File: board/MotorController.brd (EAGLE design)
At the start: 88.9 x 54.6 mm, 41 parts, among them IC1 ATMEGA328P-PU, Q1 IPP80P03P4L-04, Q2 SUP75P03-07-H, T1 BT137-600E, Y1 16Mhz

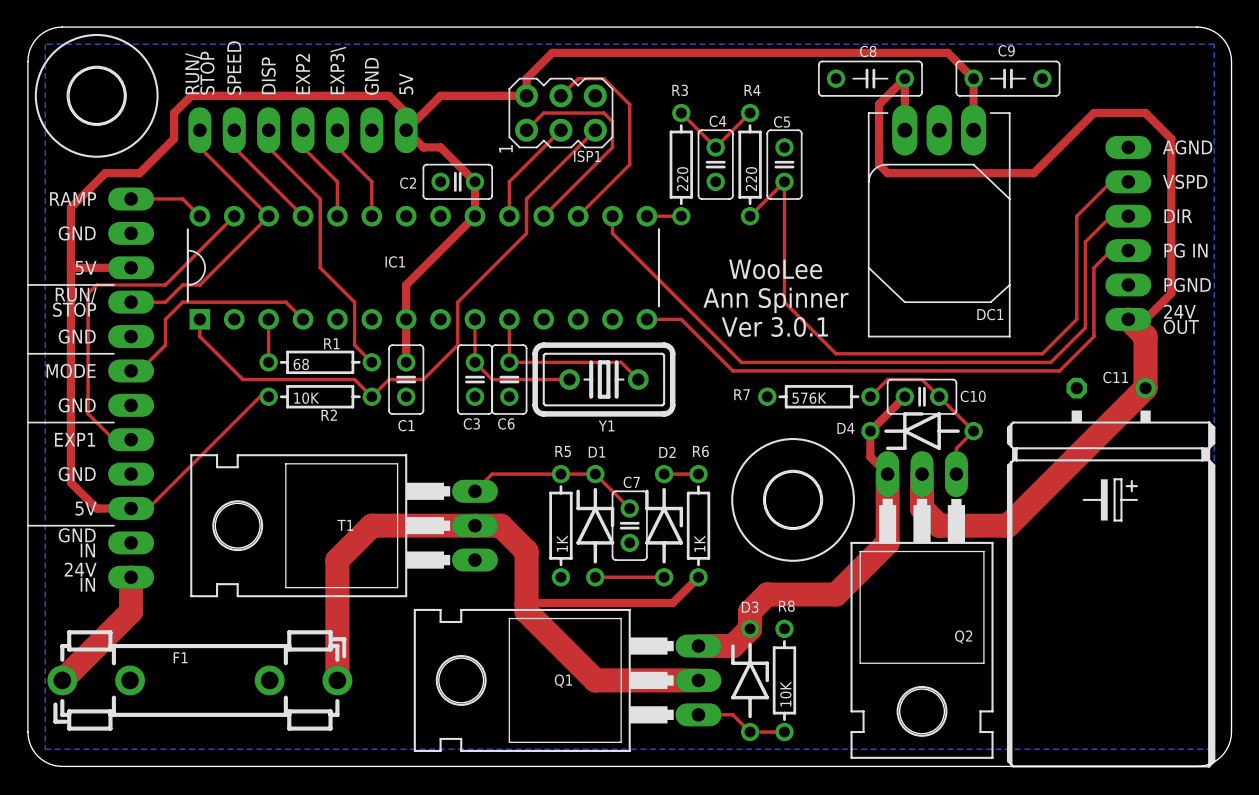
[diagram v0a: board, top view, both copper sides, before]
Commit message: Tweak TO220 packages and add board heatsink
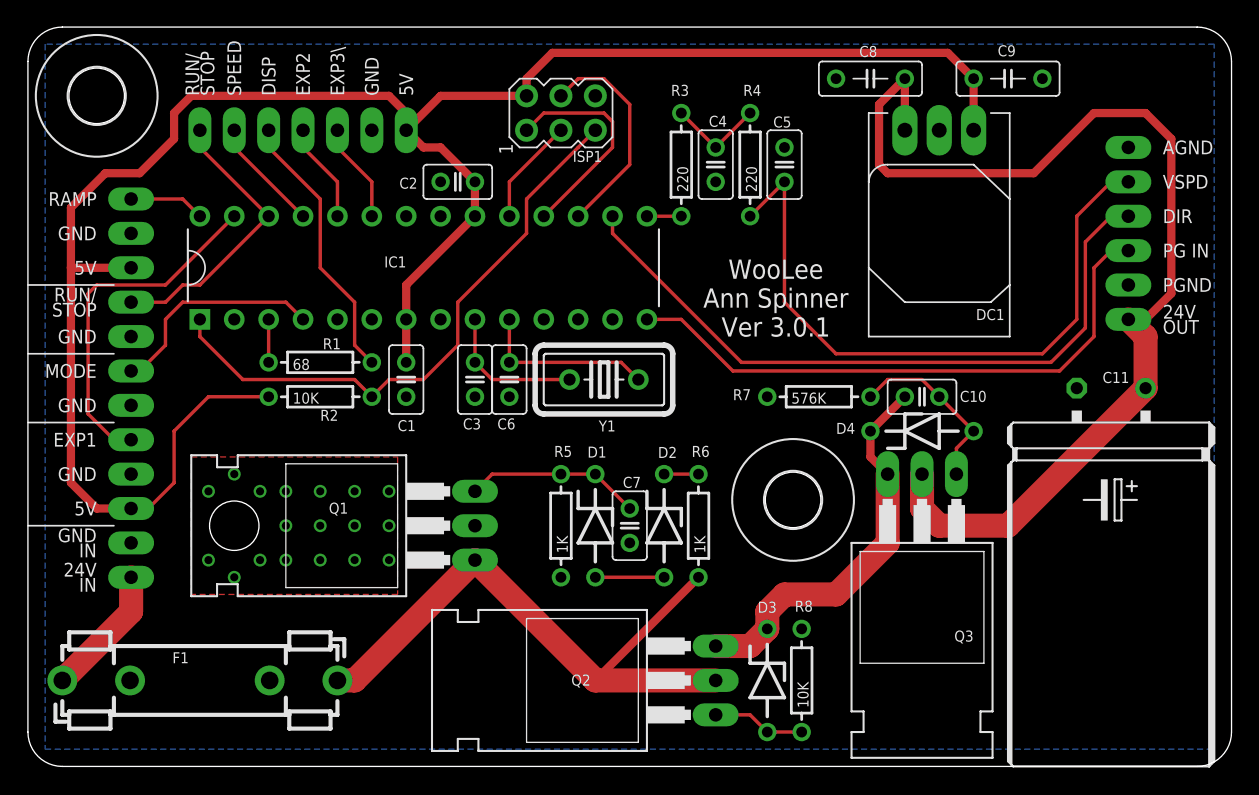
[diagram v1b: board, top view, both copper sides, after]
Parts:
- removed T1: BT137-600E, SaintGimp:TO220BH
- added Q3: SUP75P03-07-H-NH, SaintGimp:TO220BH-NO-HOLE
- Q1: value IPP80P03P4L-04 -> BT137-600E; device SaintGimp:TO220BH -> SaintGimp:TO220BH-NO-HOLE
- Q2: value SUP75P03-07-H -> IPP80P03P4L-04; device SaintGimp:TO220BH -> SaintGimp:TO220BH-NO-HOLE
- moved Q2 23.3 mm to (44.5, 6.35), turned to 90 degrees
- moved Q1 20.1 mm to (26.7, 17.8)
- moved D3 1.27 mm to (54.6, 6.35)
- moved R8 1.27 mm to (57.1, 6.35)
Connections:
- net 24V: now also Q1.P1, Q2.P2; no longer Q1.P2, T1.P2
- net 24V-PROTECTED: now also Q3.P2; no longer Q2.P2
- net GND: now also Q1.P2; no longer T1.P1
- net N$11: now also Q3.P1; no longer Q2.P1
- net N$4: now also Q2.P1; no longer Q1.P1
- net N$7: now also Q1.P3; no longer T1.P3
- net N$9: now also Q3.P3; no longer Q1.P3
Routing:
- net 24V: track 57.4 -> 46.1 mm
- net VCC: track 146.4 -> 148.6 mm
- net N$9: track 30.2 -> 29.0 mm
- added copper zone on layer 1, net GND

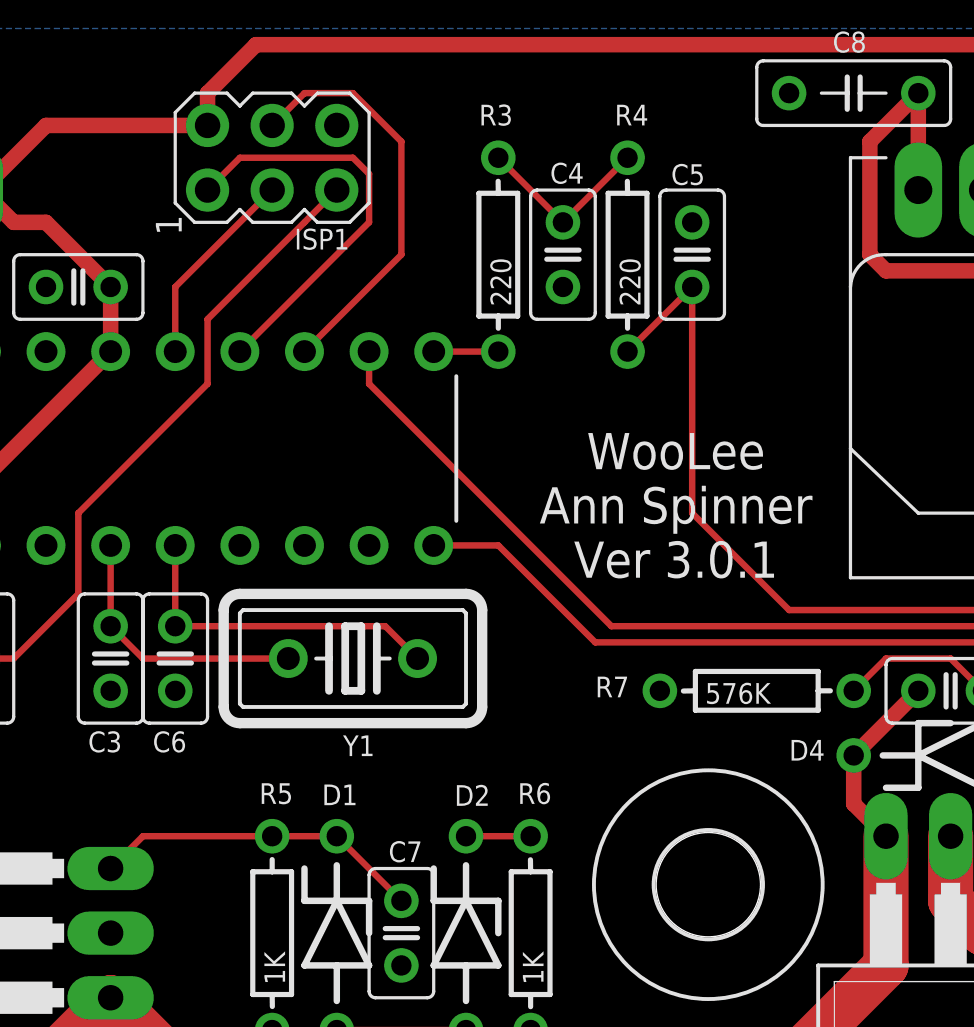
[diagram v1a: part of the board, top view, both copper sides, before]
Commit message: Fix the label order of caps
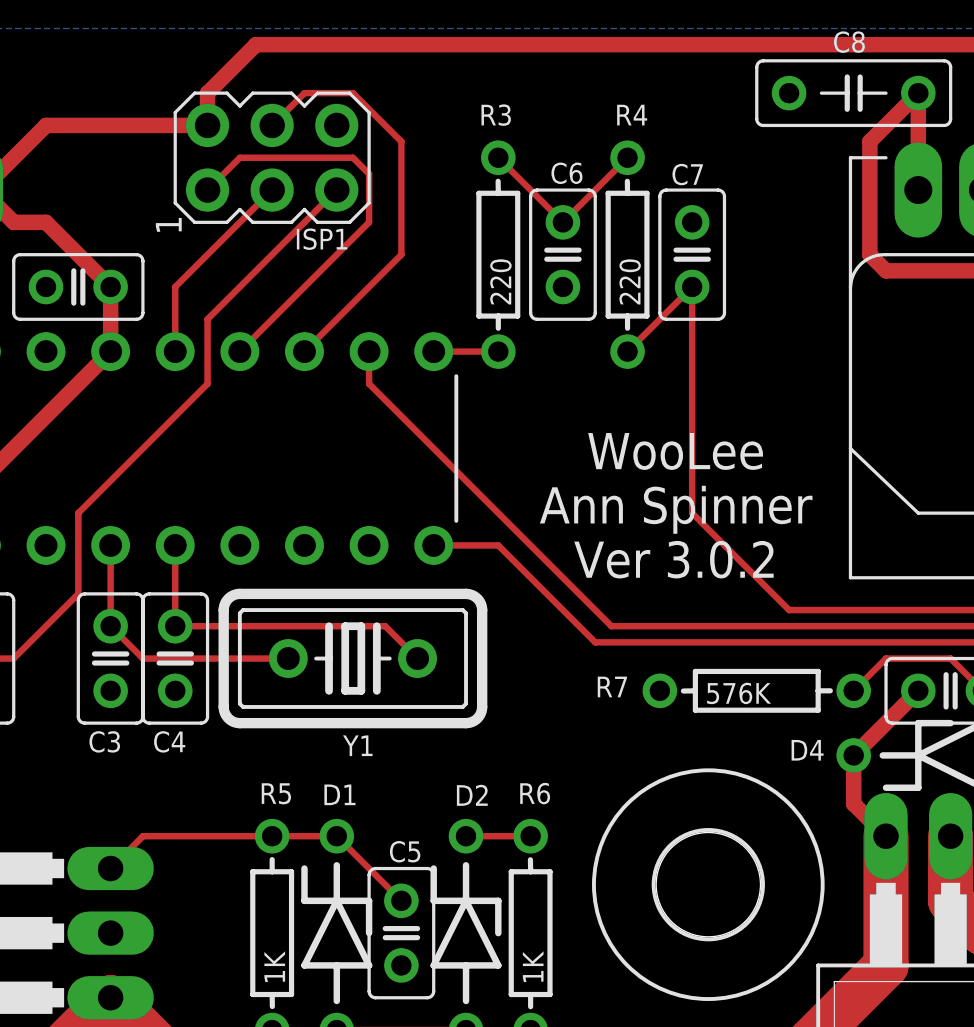
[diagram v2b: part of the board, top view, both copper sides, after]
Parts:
- C4: value 1uF -> 20pF
- C5: value 1uF -> 0.1uF
- C6: value 20pF -> 1uF
- C7: value 0.1uF -> 1uF
- moved C5 29.0 mm to (44.5, 17.8), turned to 270 degrees
- moved C7 29.0 mm to (55.9, 44.5), turned to 90 degrees
- moved C4 22.0 mm to (35.6, 28.6)
- moved C6 22.0 mm to (50.8, 44.5)
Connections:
- net CRYSTAL2: now also C4.1; no longer C6.1
- net N$1: now also C6.1; no longer C4.1
- net N$10: now also C7.1; no longer C5.1
- net N$7: now also C5.1; no longer C7.1
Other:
- board text added: "WooLee Ann Spinner Ver 3.0.2"
- board text removed: "WooLee Ann Spinner Ver 3.0.1"
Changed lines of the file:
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@@
 <text x="55.245" y="31.75" size="1.4224" layer="121" align="bottom-center">WooLee
 Ann Spinner
-Ver 3.0.1</text>
+Ver 3.0.2</text>
 <text x="5.08" y="26.67" size="1.016" layer="121" rot="SR0" align="center-right">GND</text>
 <text x="5.08" y="34.29" size="1.016" layer="121" distance="10" rot="SR0" align="center-right">RUN/
@@
 <attribute name="VALUE" x="50.038" y="15.748" size="0.8128" layer="21" ratio="10" rot="R90"/>
 </element>
-<element name="C7" library="SaintGimp" package="CAPACITOR-2.5MM" value="0.1uF" x="44.45" y="17.78" smashed="yes" rot="R270">
+<element name="C5" library="SaintGimp" package="CAPACITOR-2.5MM" value="0.1uF" x="44.45" y="17.78" smashed="yes" rot="R270">
 <attribute name="NAME" x="43.942" y="20.574" size="0.8128" layer="25"/>
 <attribute name="VALUE" x="42.164" y="19.685" size="0.8128" layer="27" rot="R270"/>
@@
 <attribute name="VALUE" x="53.848" y="42.418" size="0.8128" layer="21" ratio="10" rot="R90"/>
 </element>
-<element name="C4" library="SaintGimp" package="CAPACITOR-2.5MM" value="1uF" x="50.8" y="44.45" smashed="yes" rot="R270">
+<element name="C6" library="SaintGimp" package="CAPACITOR-2.5MM" value="1uF" x="50.8" y="44.45" smashed="yes" rot="R270">
 <attribute name="NAME" x="50.292" y="47.244" size="0.8128" layer="25"/>
 <attribute name="VALUE" x="48.514" y="46.355" size="0.8128" layer="27" rot="R270"/>
 </element>
-<element name="C5" library="SaintGimp" package="CAPACITOR-2.5MM" value="1uF" x="55.88" y="44.45" smashed="yes" rot="R90">
+<element name="C7" library="SaintGimp" package="CAPACITOR-2.5MM" value="1uF" x="55.88" y="44.45" smashed="yes" rot="R90">
 <attribute name="NAME" x="56.388" y="48.006" size="0.8128" layer="25" rot="R180"/>
 <attribute name="VALUE" x="58.166" y="42.672" size="0.8128" layer="27" rot="R90"/>
@@
 <attribute name="VALUE" x="30.734" y="29.083" size="0.8128" layer="27" rot="R270"/>
 </element>
-<element name="C6" library="SaintGimp" package="CAPACITOR-2.5MM" value="20pF" x="35.56" y="28.575" smashed="yes" rot="R270">
+<element name="C4" library="SaintGimp" package="CAPACITOR-2.5MM" value="20pF" x="35.56" y="28.575" smashed="yes" rot="R270">
 <attribute name="NAME" x="34.671" y="24.892" size="0.8128" layer="25"/>
 <attribute name="VALUE" x="33.274" y="30.353" size="0.8128" layer="27" rot="R270"/>
@@
 <contactref element="Q1" pad="P2"/>
 <contactref element="R5" pad="P$1"/>
-<contactref element="C7" pad="2"/>
+<contactref element="C5" pad="2"/>
 <contactref element="R8" pad="P$1"/>
 <contactref element="24VIN" pad="1"/>
 <contactref element="C9" pad="2"/>
 <contactref element="24VOUT" pad="2"/>
-<contactref element="C5" pad="2"/>
+<contactref element="C7" pad="2"/>
 <contactref element="C1" pad="1"/>
 <contactref element="C3" pad="2"/>
+<contactref element="C4" pad="2"/>
 <contactref element="C6" pad="2"/>
-<contactref element="C4" pad="2"/>
-<contactref element="C4" pad="2"/>
+<contactref element="C6" pad="2"/>
 <contactref element="DC1" pad="P2"/>
 <polygon width="0.4064" layer="16" isolate="0.2794">
@@
 <contactref element="Q1" pad="P3"/>
 <contactref element="D1" pad="C"/>
-<contactref element="C7" pad="1"/>
+<contactref element="C5" pad="1"/>
 <contactref element="R5" pad="P$2"/>
 <wire x1="39.37" y1="21.59" x2="41.91" y2="21.59" width="0.254" layer="1"/>
@@
 <signal name="N$10">
 <contactref element="R4" pad="P$2"/>
-<contactref element="C5" pad="1"/>
+<contactref element="C7" pad="1"/>
 <contactref element="MOTOR" pad="3"/>
 <wire x1="53.34" y1="40.64" x2="55.88" y2="43.18" width="0.254" layer="1"/>
@@
 <signal name="CRYSTAL2">
 <contactref element="Y1" pad="1"/>
-<contactref element="C6" pad="1"/>
+<contactref element="C4" pad="1"/>
 <contactref element="IC1" pad="10"/>
 <wire x1="45.085" y1="28.575" x2="43.815" y2="29.845" width="0.254" layer="1"/>
@@
 <contactref element="R3" pad="P$1"/>
 <contactref element="R4" pad="P$1"/>
-<contactref element="C4" pad="1"/>
+<contactref element="C6" pad="1"/>
 <wire x1="48.26" y1="48.26" x2="50.8" y2="45.72" width="0.254" layer="1"/>
 <wire x1="50.8" y1="45.72" x2="53.34" y2="48.26" width="0.254" layer="1"/>

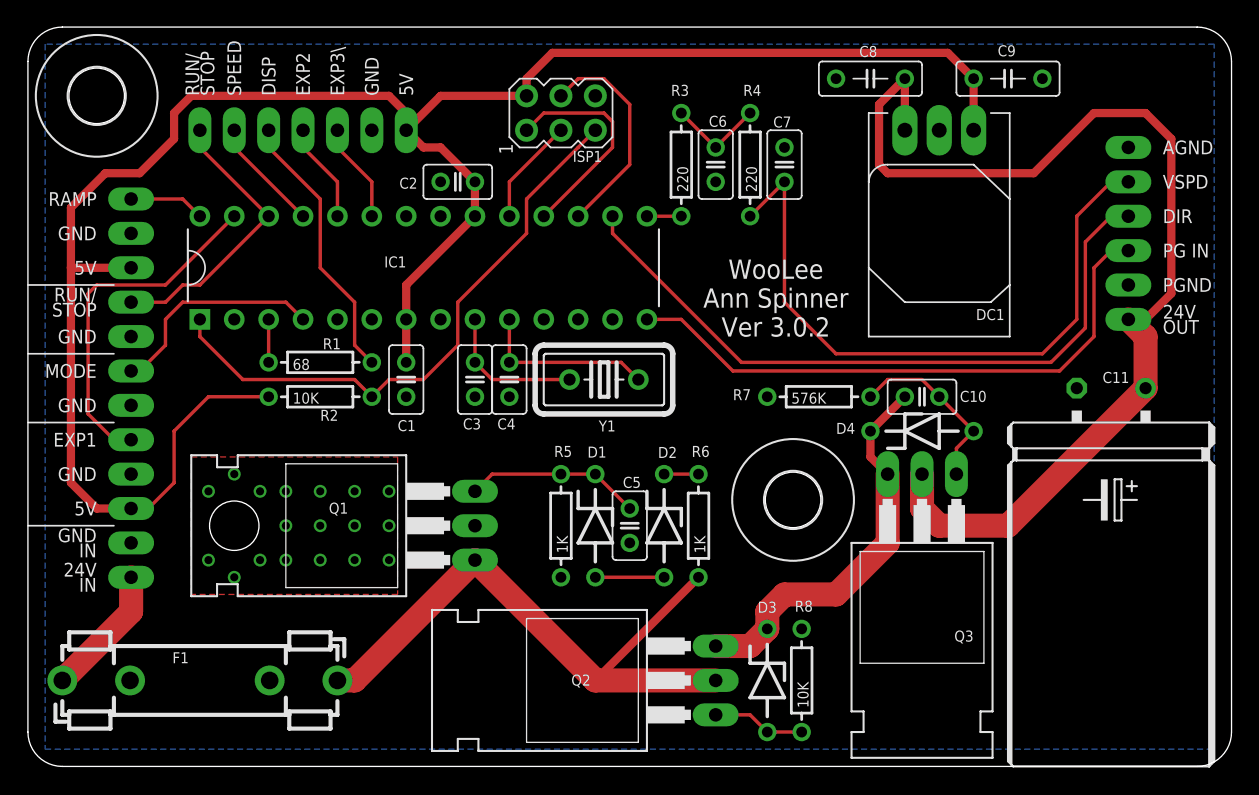
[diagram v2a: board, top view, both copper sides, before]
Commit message: Revert back to previous triac circuit
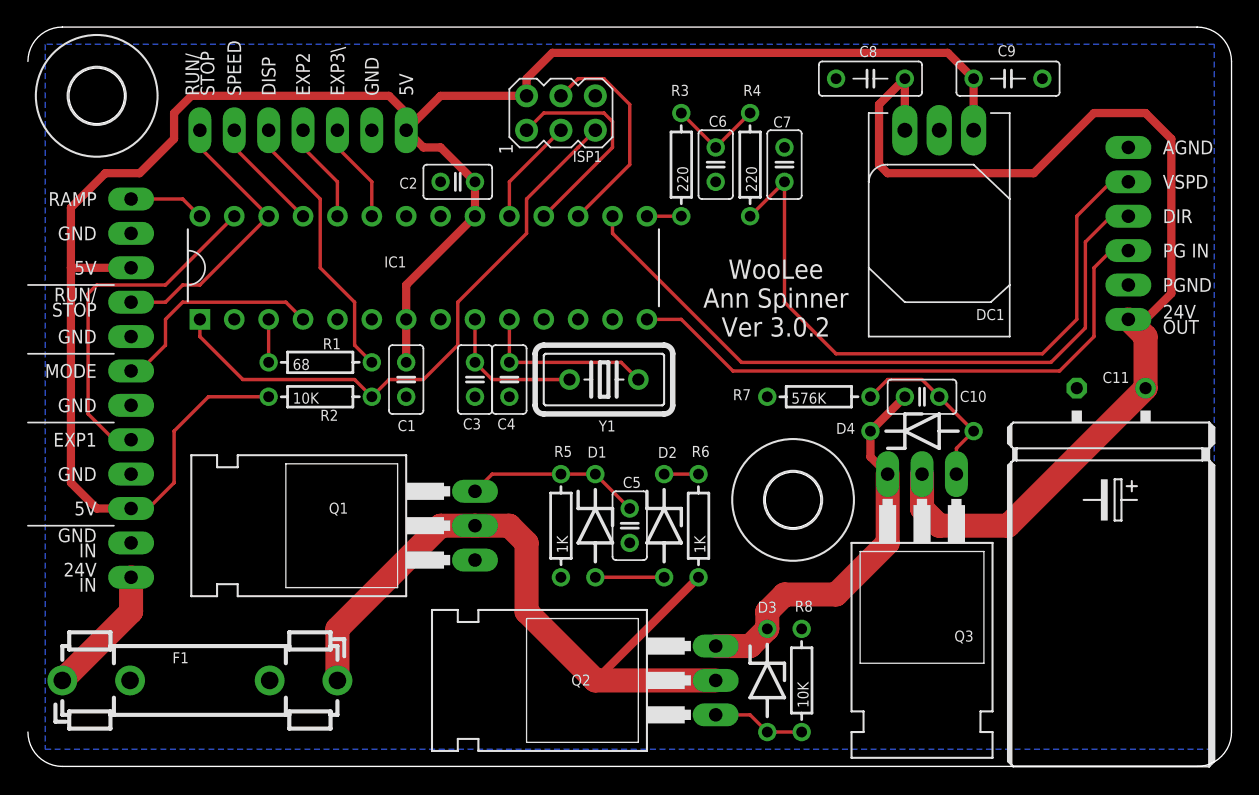
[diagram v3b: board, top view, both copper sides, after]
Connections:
- net 24V: now also Q1.P2; no longer Q1.P1
- net GND: now also Q1.P1; no longer Q1.P2
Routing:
- net 24V: track 46.1 -> 53.4 mm
- removed copper zone on layer 1, net GND
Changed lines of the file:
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@@
 <board>
 <plain>
-<wire x1="0" y1="52.07" x2="0" y2="2.54" width="0" layer="20"/>
 <wire x1="0" y1="2.54" x2="2.54" y2="0" width="0" layer="20" curve="90"/>
 <wire x1="2.54" y1="0" x2="86.36" y2="0" width="0" layer="20"/>
@@
 <wire x1="54.61" y1="54.61" x2="54.61" y2="0" width="0.127" layer="51" style="shortdash"/>
 <wire x1="48.26" y1="54.61" x2="48.26" y2="0" width="0.127" layer="51" style="shortdash"/>
-<hole x="15.24" y="17.78" drill="3.65000625"/>
 </plain>
 <attributes>
@@
 <signal name="GND">
 <contactref element="C11" pad="-"/>
-<contactref element="Q1" pad="P2"/>
+<contactref element="Q1" pad="P1"/>
 <contactref element="R5" pad="P$1"/>
 <contactref element="C5" pad="2"/>
@@
 <contactref element="SIDE_EXP" pad="2"/>
 <contactref element="R7" pad="P$1"/>
-<via x="15.24" y="21.59" extent="1-16" drill="0.6"/>
-<via x="15.24" y="13.97" extent="1-16" drill="0.6"/>
-<via x="13.335" y="20.32" extent="1-16" drill="0.6"/>
-<polygon width="0.254" layer="1">
-<vertex x="12.065" y="22.86"/>
-<vertex x="27.305" y="22.86"/>
-<vertex x="27.305" y="22.225"/>
-<vertex x="27.305" y="12.7"/>
-<vertex x="12.065" y="12.7"/>
-</polygon>
-<via x="17.145" y="20.32" extent="1-16" drill="0.6"/>
-<via x="19.05" y="20.32" extent="1-16" drill="0.6"/>
-<via x="21.59" y="20.32" extent="1-16" drill="0.6"/>
-<via x="24.13" y="20.32" extent="1-16" drill="0.6"/>
-<via x="26.67" y="20.32" extent="1-16" drill="0.6"/>
-<via x="26.67" y="17.78" extent="1-16" drill="0.6"/>
-<via x="26.67" y="15.24" extent="1-16" drill="0.6"/>
-<via x="24.13" y="15.24" extent="1-16" drill="0.6"/>
-<via x="17.145" y="15.24" extent="1-16" drill="0.6"/>
-<via x="19.05" y="15.24" extent="1-16" drill="0.6"/>
-<via x="21.59" y="15.24" extent="1-16" drill="0.6"/>
-<via x="13.335" y="15.24" extent="1-16" drill="0.6"/>
-<via x="19.05" y="17.78" extent="1-16" drill="0.6"/>
-<via x="21.59" y="17.78" extent="1-16" drill="0.6"/>
-<via x="24.13" y="17.78" extent="1-16" drill="0.6"/>
 </signal>
 <signal name="N$5">
@@
 <contactref element="F1" pad="2"/>
 <contactref element="R6" pad="P$2"/>
-<contactref element="Q1" pad="P1"/>
+<contactref element="Q1" pad="P2"/>
 <contactref element="Q2" pad="P2"/>
-<wire x1="33.02" y1="15.24" x2="41.91" y2="6.35" width="1.778" layer="1"/>
 <wire x1="41.91" y1="6.35" x2="50.8" y2="6.35" width="1.778" layer="1"/>
 <wire x1="49.53" y1="13.97" x2="41.91" y2="6.35" width="0.6096" layer="1"/>
-<wire x1="22.86" y1="6.35" x2="24.13" y2="6.35" width="1.778" layer="1"/>
-<wire x1="24.13" y1="6.35" x2="33.02" y2="15.24" width="1.778" layer="1"/>
+<wire x1="22.86" y1="6.35" x2="22.86" y2="10.16" width="1.778" layer="1"/>
+<wire x1="22.86" y1="10.16" x2="30.48" y2="17.78" width="1.778" layer="1"/>
+<wire x1="30.48" y1="17.78" x2="33.02" y2="17.78" width="1.778" layer="1"/>
+<wire x1="33.02" y1="17.78" x2="35.56" y2="17.78" width="1.778" layer="1"/>
+<wire x1="35.56" y1="17.78" x2="36.83" y2="16.51" width="1.778" layer="1"/>
+<wire x1="36.83" y1="16.51" x2="36.83" y2="11.43" width="1.778" layer="1"/>
+<wire x1="36.83" y1="11.43" x2="41.91" y2="6.35" width="1.778" layer="1"/>
 </signal>
 <signal name="N$4">
